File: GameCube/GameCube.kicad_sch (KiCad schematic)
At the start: 18 parts, among them J1 Conn_01x03_Pin, J2 Conn_01x03_Pin, J3 Conn_01x03_Pin, J4 Conn_01x03_Pin, J5 Conn_01x02_Pin, J6 Conn_01x02_Pin, J7 Conn_01x02_Pin, U1 ESP32-C3-DevKitM-1

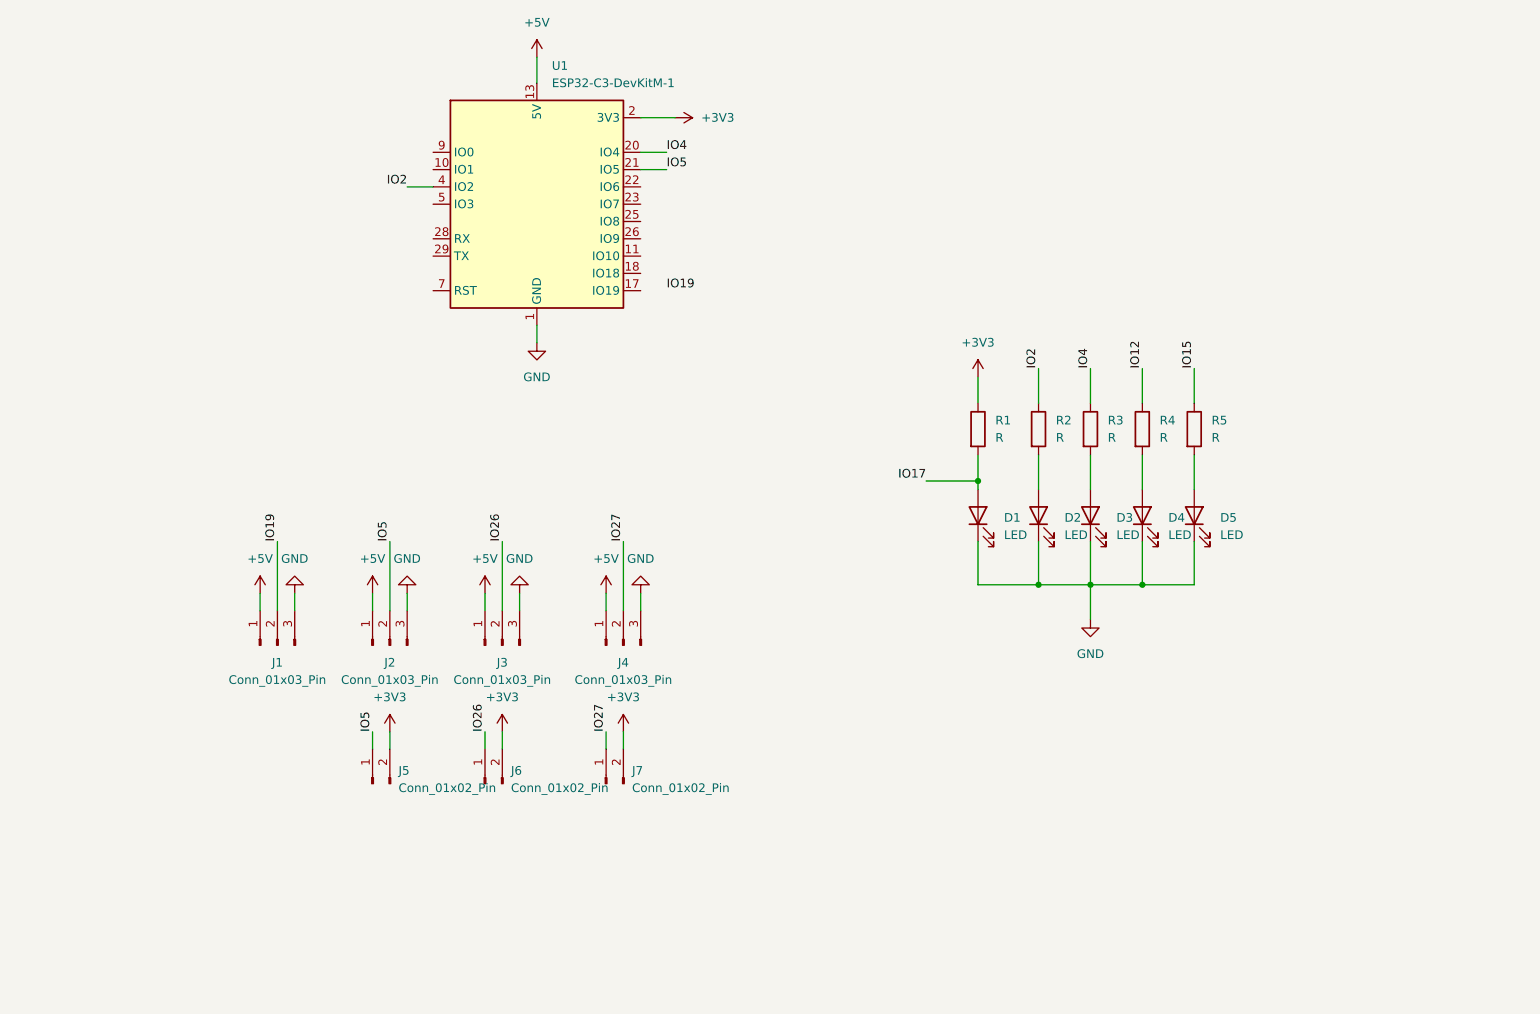
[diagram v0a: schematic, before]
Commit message: Add esp32 footprints and pcb outline
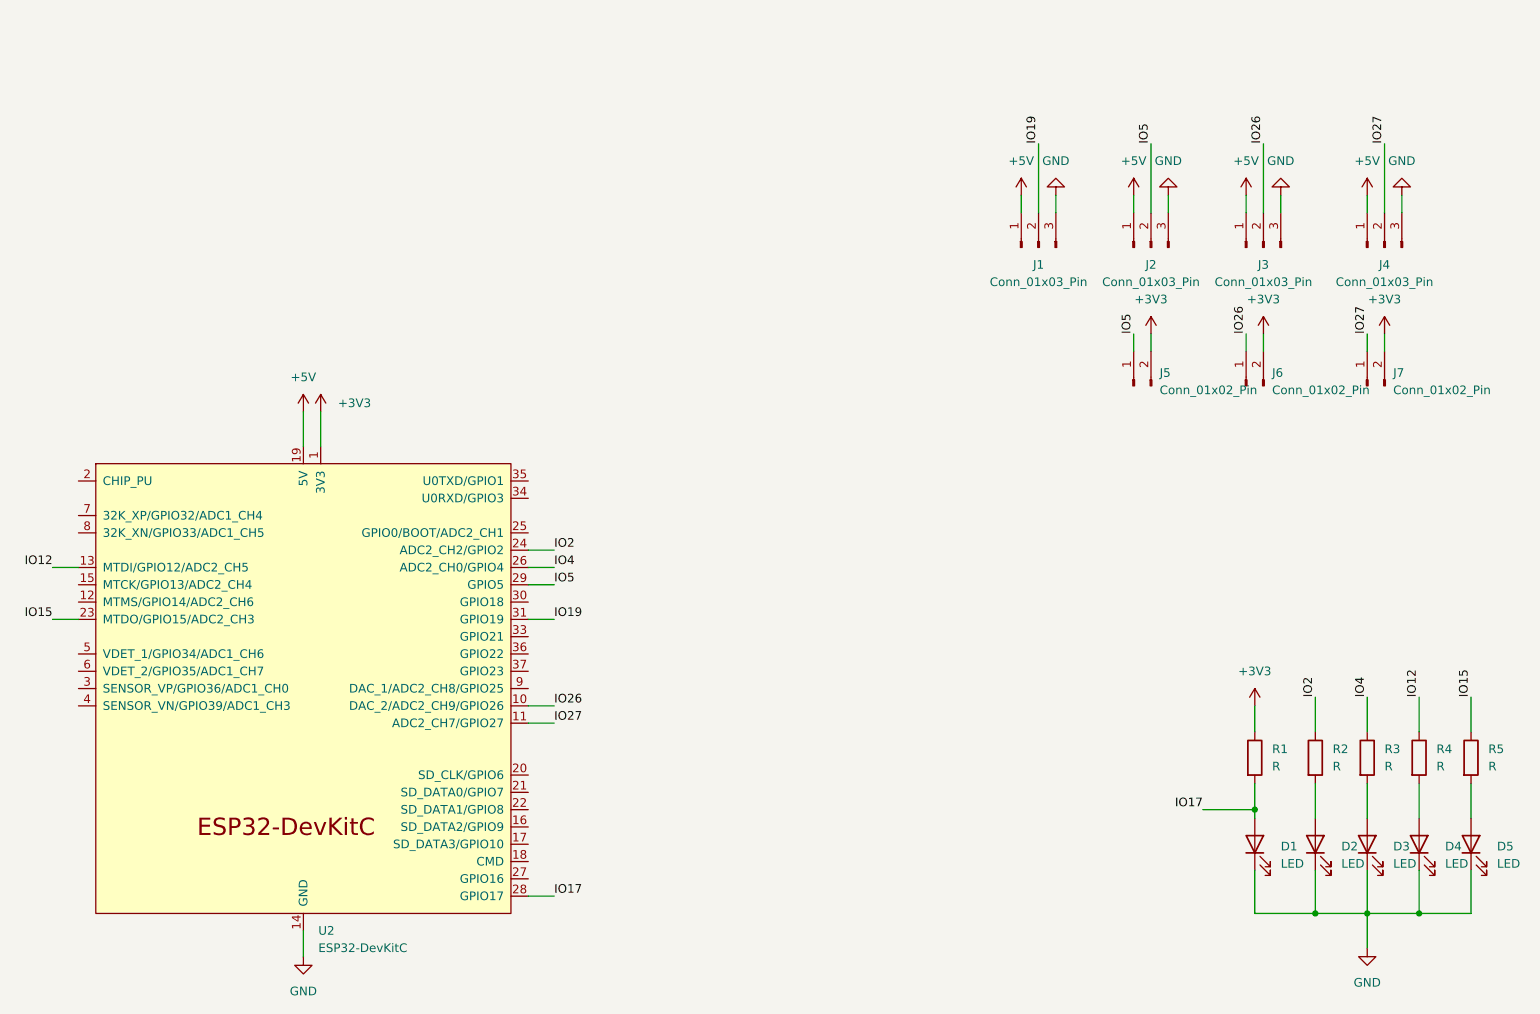
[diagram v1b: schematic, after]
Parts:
- removed U1: ESP32-C3-DevKitM-1, RF_Module:ESP32-C3-DevKitM-1, symbol RF_Module:ESP32-C3-DevKitM-1
- added U2: ESP32-DevKitC, PCM_Espressif:ESP32-DevKitC, symbol PCM_Espressif:ESP32-DevKitC
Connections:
- net +3V3: now also U2.1 (3V3)
- net +5V: now also U2.19 (5V)
- net GND: now also U2.14 (GND), U2.32 (GND), U2.38 (GND)
- net IO12: now also U2.13 (MTDI/GPIO12/ADC2_CH5)
- net IO15: now also U2.23 (MTDO/GPIO15/ADC2_CH3)
- net IO17: now also U2.28 (GPIO17)
- net IO19: now also U2.31 (GPIO19)
- net IO2: now also U2.24 (ADC2_CH2/GPIO2)
- net IO26: now also U2.10 (DAC_2/ADC2_CH9/GPIO26)
- net IO27: now also U2.11 (ADC2_CH7/GPIO27)
- net IO4: now also U2.26 (ADC2_CH0/GPIO4)
- net IO5: now also U2.29 (GPIO5)
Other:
- moved on the sheet: D1, D2, D3, D4, D5, J1, J2, J3, J4, J5, J6, J7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
